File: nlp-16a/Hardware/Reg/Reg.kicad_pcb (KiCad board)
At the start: 2 copper layers, 209.6 x 154.9 mm, 136 parts, among them J1 Conn_02x20_Odd_Even, J2 Conn_02x20_Odd_Even, J3 Conn_02x20_Odd_Even, J4 Conn_02x20_Odd_Even, J5 Conn_02x16_Odd_Even, J6 Conn_02x16_Odd_Even, J7 Screw_Terminal_01x02, J8 Conn_02x10_Odd_Even, U1 CD74HC00, U10 CD74HC00, U11 CD74HC00, U12 CD74HC00, U13 CD74HC00, U14 CD74HC00, U15 CD74HC00, U16 CD74HC00, U17 CD74HC00, U18 CD74HC00, U19 CD74HC00, U2 CD74HC00, U20 CD74HC00, U21 CD74HC00, U22 CD74HC00, U23 CD74HC00, U24 CD74HC00, U25 CD74HC00, U26 CD74HC00, U27 CD74HC00, U28 CD74HC00, U29 CD74HC00, U3 CD74HC00, U30 CD74HC00, U31 CD74HC00, U32 CD74HC00, U33 CD74HC00, U34 CD74HC00, U35 CD74HC00, U4 CD74HC00, U5 CD74HC00, U6 CD74HC00, U7 CD74HC00, U8 CD74HC00, U9 CD74HC00

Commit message: レジスタ基板だいたい完成
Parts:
- added C18: C, Capacitor_THT:C_Disc_D7.5mm_W2.5mm_P5.00mm, F.Cu at (225.4, 53.4)
- added C19: C, Capacitor_THT:C_Disc_D7.5mm_W2.5mm_P5.00mm, F.Cu at (225.4, 66.1)
- added G***: LOGO, LOGO, F.Cu at (190.5, 45.1)
- added JP17: Jumper_3_Bridged12, Jumper:SolderJumper-3_P1.3mm_Bridged12_RoundedPad1.0x1.5mm_NumberLabels, F.Cu at (238.8, 82.5)
- added R36: R, Resistor_SMD:R_0603_1608Metric_Pad0.98x0.95mm_HandSolder, F.Cu at (206.4, 49.5)
- added R37: R, Resistor_SMD:R_0603_1608Metric_Pad0.98x0.95mm_HandSolder, F.Cu at (202.6, 49.5)
- added U36: CD74HC00, Package_DIP:DIP-14_W7.62mm, F.Cu at (228.6, 73.7)
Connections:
- net ALL_SEL_in renamed CLR_in
- D1 pad 2: /Register/Reg0/Q -> Reg_out0
- D10 pad 2: /Register/Reg9/Q -> Reg_out9
- D11 pad 2: /Register/Reg10/Q -> Reg_out10
- D12 pad 2: /Register/Reg11/Q -> Reg_out11
- D13 pad 2: /Register/Reg12/Q -> Reg_out12
- D14 pad 2: /Register/Reg13/Q -> Reg_out13
- D15 pad 2: /Register/Reg14/Q -> Reg_out14
- D16 pad 2: /Register/Reg15/Q -> Reg_out15
- D19 pad 2: Net-(U10-Pad2) -> Net-(U34-Pad11)
- D2 pad 2: /Register/Reg1/Q -> Reg_out1
- D3 pad 2: /Register/Reg2/Q -> Reg_out2
- D4 pad 2: /Register/Reg3/Q -> Reg_out3
- D5 pad 2: /Register/Reg4/Q -> Reg_out4
- D6 pad 2: /Register/Reg5/Q -> Reg_out5
- D7 pad 2: /Register/Reg6/Q -> Reg_out6
- D8 pad 2: /Register/Reg7/Q -> Reg_out7
- D9 pad 2: /Register/Reg8/Q -> Reg_out8
- J1 pad 36: phi1 -> phi1_in
- J3 pad 33: ALL_SEL_out -> CLR_out
- J3 pad 36: phi1 -> phi1_out
- J8 pad 10: Address2 -> Reg_out2
- J8 pad 11: Address11 -> Reg_out11
- J8 pad 12: Address3 -> Reg_out3
- J8 pad 13: Address12 -> Reg_out12
- J8 pad 14: Address4 -> Reg_out4
- J8 pad 15: Address13 -> Reg_out13
- J8 pad 16: Address5 -> Reg_out5
- J8 pad 17: Address14 -> Reg_out14
- J8 pad 18: Address6 -> Reg_out6
- J8 pad 19: Address15 -> Reg_out15
- J8 pad 20: Address7 -> Reg_out7
- J8 pad 5: Address8 -> Reg_out8
- J8 pad 6: Address0 -> Reg_out0
- J8 pad 7: Address9 -> Reg_out9
- J8 pad 8: Address1 -> Reg_out1
- J8 pad 9: Address10 -> Reg_out10
- U1 pad 2: VCC -> Net-(U8-Pad5)
- U1 pad 5: VCC -> Net-(U8-Pad5)
- U10 pad 10: /Register/Reg12/Q -> Reg_out12
- U10 pad 13: /Register/Reg13/Q -> Reg_out13
- U11 pad 10: /Register/Reg10/Q -> Reg_out10
- U11 pad 13: /Register/Reg11/Q -> Reg_out11
- U12 pad 10: /Register/Reg8/Q -> Reg_out8
- U12 pad 13: /Register/Reg9/Q -> Reg_out9
- U13 pad 10: /Register/Reg6/Q -> Reg_out6
- U13 pad 13: /Register/Reg7/Q -> Reg_out7
- U14 pad 10: /Register/Reg4/Q -> Reg_out4
- U14 pad 13: /Register/Reg5/Q -> Reg_out5
- U15 pad 10: /Register/Reg2/Q -> Reg_out2
- U15 pad 13: /Register/Reg3/Q -> Reg_out3
- U16 pad 10: /Register/Reg0/Q -> Reg_out0
- U16 pad 13: /Register/Reg1/Q -> Reg_out1
- U17 pad 10: /Register/Reg15/Q -> Reg_out15
- U17 pad 11: /Register/Reg15/Q -> Reg_out15
- U18 pad 10: /Register/Reg13/Q -> Reg_out13
- U18 pad 11: /Register/Reg13/Q -> Reg_out13
- U19 pad 10: /Register/Reg11/Q -> Reg_out11
- U19 pad 11: /Register/Reg11/Q -> Reg_out11
- U2 pad 2: VCC -> Net-(U8-Pad5)
- U2 pad 5: VCC -> Net-(U8-Pad5)
- U20 pad 10: /Register/Reg9/Q -> Reg_out9
- U20 pad 11: /Register/Reg9/Q -> Reg_out9
- U21 pad 10: /Register/Reg7/Q -> Reg_out7
- U21 pad 11: /Register/Reg7/Q -> Reg_out7
- U22 pad 10: /Register/Reg5/Q -> Reg_out5
- U22 pad 11: /Register/Reg5/Q -> Reg_out5
- U23 pad 10: /Register/Reg3/Q -> Reg_out3
- U23 pad 11: /Register/Reg3/Q -> Reg_out3
- U24 pad 10: /Register/Reg1/Q -> Reg_out1
- U24 pad 11: /Register/Reg1/Q -> Reg_out1
- U25 pad 10: /Register/Reg14/Q -> Reg_out14
- U25 pad 11: /Register/Reg14/Q -> Reg_out14
- U26 pad 10: /Register/Reg12/Q -> Reg_out12
- U26 pad 11: /Register/Reg12/Q -> Reg_out12
- U27 pad 10: /Register/Reg10/Q -> Reg_out10
- U27 pad 11: /Register/Reg10/Q -> Reg_out10
- U28 pad 10: /Register/Reg8/Q -> Reg_out8
- U28 pad 11: /Register/Reg8/Q -> Reg_out8
- U29 pad 10: /Register/Reg6/Q -> Reg_out6
- U29 pad 11: /Register/Reg6/Q -> Reg_out6
- U3 pad 2: VCC -> Net-(U8-Pad5)
- U3 pad 5: VCC -> Net-(U8-Pad5)
- U30 pad 10: /Register/Reg4/Q -> Reg_out4
- U30 pad 11: /Register/Reg4/Q -> Reg_out4
- U31 pad 10: /Register/Reg2/Q -> Reg_out2
- U31 pad 11: /Register/Reg2/Q -> Reg_out2
- U32 pad 10: /Register/Reg0/Q -> Reg_out0
- U32 pad 11: /Register/Reg0/Q -> Reg_out0
- U33 pad 10: ALL_SEL_out -> Net-(U33-Pad5)
- U33 pad 5: ALL_SEL_out -> Net-(U33-Pad5)
- U34 pad 11: Net-(U10-Pad2) -> Net-(U34-Pad11)
- U35 pad 8: ALL_SEL_out -> CLR_out
- U4 pad 2: VCC -> Net-(U8-Pad5)
- U4 pad 5: VCC -> Net-(U8-Pad5)
- U5 pad 2: VCC -> Net-(U8-Pad5)
- U5 pad 5: VCC -> Net-(U8-Pad5)
- U6 pad 2: VCC -> Net-(U8-Pad5)
- U6 pad 5: VCC -> Net-(U8-Pad5)
- U7 pad 2: VCC -> Net-(U8-Pad5)
- U7 pad 5: VCC -> Net-(U8-Pad5)
- U8 pad 2: VCC -> Net-(U8-Pad5)
- U8 pad 5: VCC -> Net-(U8-Pad5)
- U9 pad 10: /Register/Reg14/Q -> Reg_out14
- U9 pad 13: /Register/Reg15/Q -> Reg_out15
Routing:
- net Net-(U34-Pad11): track 0.00 -> 328.5 mm, vias 0 -> 2
- net Net-(U8-Pad5): track 0.00 -> 266.3 mm
- net Reg_out1: track 0.00 -> 179.0 mm, vias 0 -> 2
- net Reg_out0: track 0.00 -> 177.6 mm, vias 0 -> 2
- net Reg_out3: track 0.00 -> 174.7 mm, vias 0 -> 2
- net Reg_out2: track 0.00 -> 173.8 mm, vias 0 -> 2
- net Reg_out5: track 0.00 -> 167.9 mm, vias 0 -> 2
- net Reg_out4: track 0.00 -> 167.3 mm, vias 0 -> 2
- net Reg_out14: track 0.00 -> 165.8 mm, vias 0 -> 3
- net Reg_out7: track 0.00 -> 165.6 mm, vias 0 -> 2
- net Reg_out6: track 0.00 -> 165.6 mm, vias 0 -> 2
- net Reg_out15: track 0.00 -> 165.2 mm, vias 0 -> 3
- net CLR_out: track 0.00 -> 162.4 mm, vias 0 -> 1
- net ALL_SEL_out: track 158.3 -> 0.00 mm, vias 1 -> 0
- net /Register/Reg14/Q: track 157.0 -> 0.00 mm
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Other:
- board text added: "+ -"
- board text added: "0 --------------ID-------------- F"
- board text added: "0 -------------ID--------------- F"
- board text added: "0 ------------Data------------- F 0 -----------Address------------ F"
- board text added: "16bit Reg"
- board text added: "3 2 1 0"
- board text added: "7 6 5 4"
- board text added: "A BUS"
- board text added: "ALL φ1 φ2"
- board text added: "B A 9 8"
- board text added: "B D x x"
- board text added: "Buf, Data CLR"
- board text added: "Ctrl"
- board text added: "Data"
- board text added: "F ------------- 8 7 ------------- 0"
- board text added: "F E D C"
- board text added: "MUX"
- board text added: "NLP-16A 16bit Register v1.0 S/N:007-0001"
- board text added: "PWR"
- board text added: "RD"
- board text added: "Reg OUTPUT PORT"
- board text added: "Vcc GND"
- board text added: "WR"
- board text added: "Y BUS"
- board text added: "unbuf : short"
- board text added: "↑IR2 short 2-3 cut 1-2"

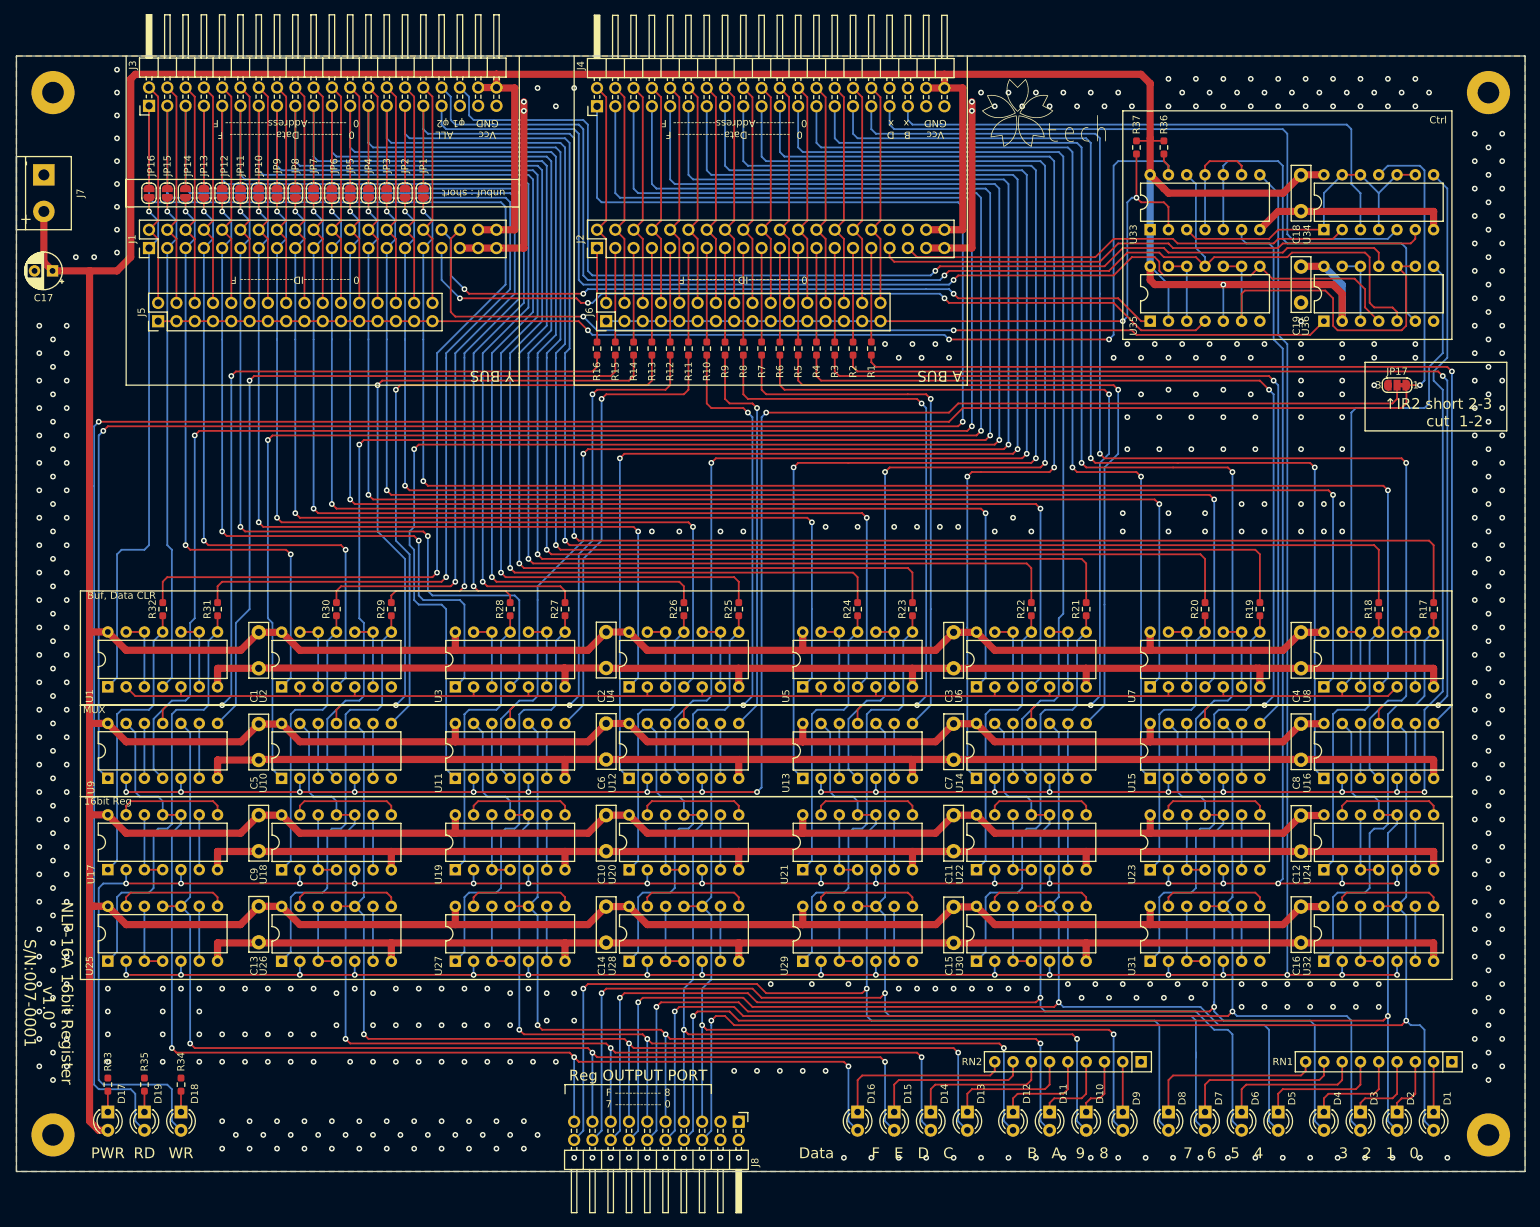
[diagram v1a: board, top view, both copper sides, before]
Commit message: テストを受けてレジスタの設計を更新
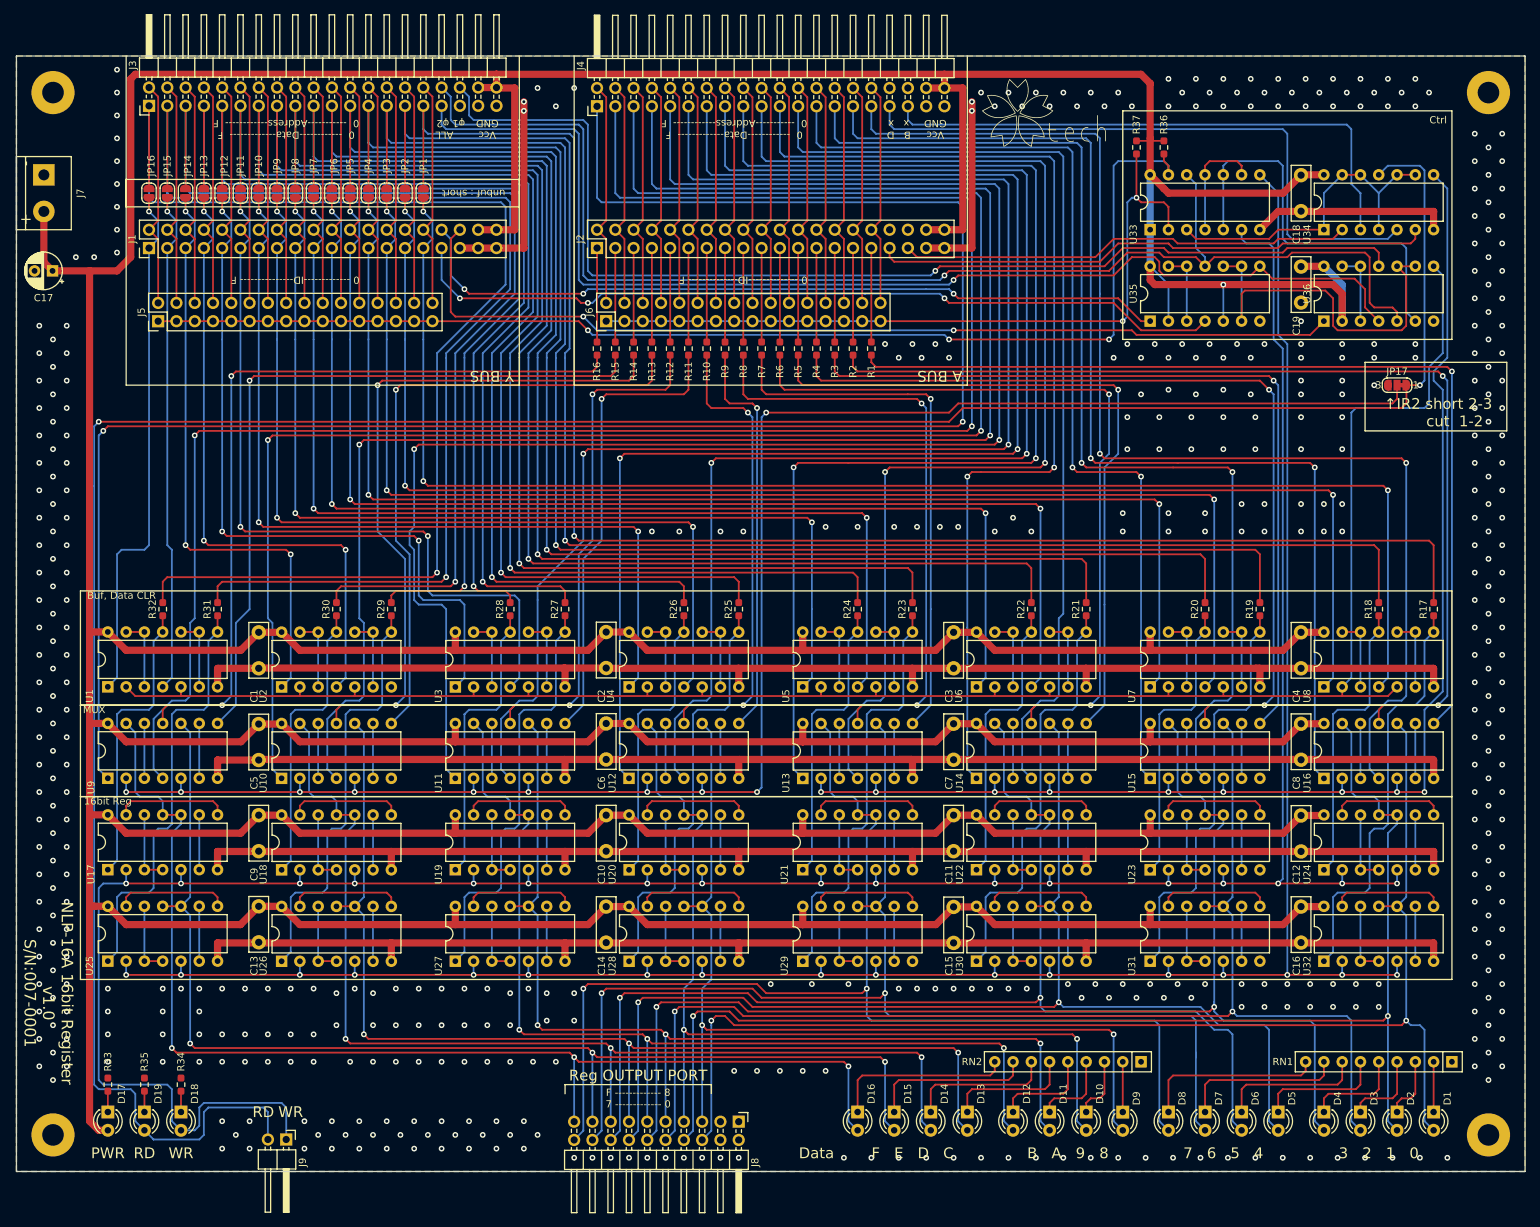
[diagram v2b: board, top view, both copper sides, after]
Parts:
- added J9: Conn_01x02_Male, Connector_PinHeader_2.54mm:PinHeader_1x02_P2.54mm_Horizontal, F.Cu at (84.5, 187.3)
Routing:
- net Net-(D19-Pad2): track 328.5 -> 354.0 mm
- net /Register/Reg1/Gate: track 350.0 -> 372.4 mm
- net GND: vias 499 -> 495

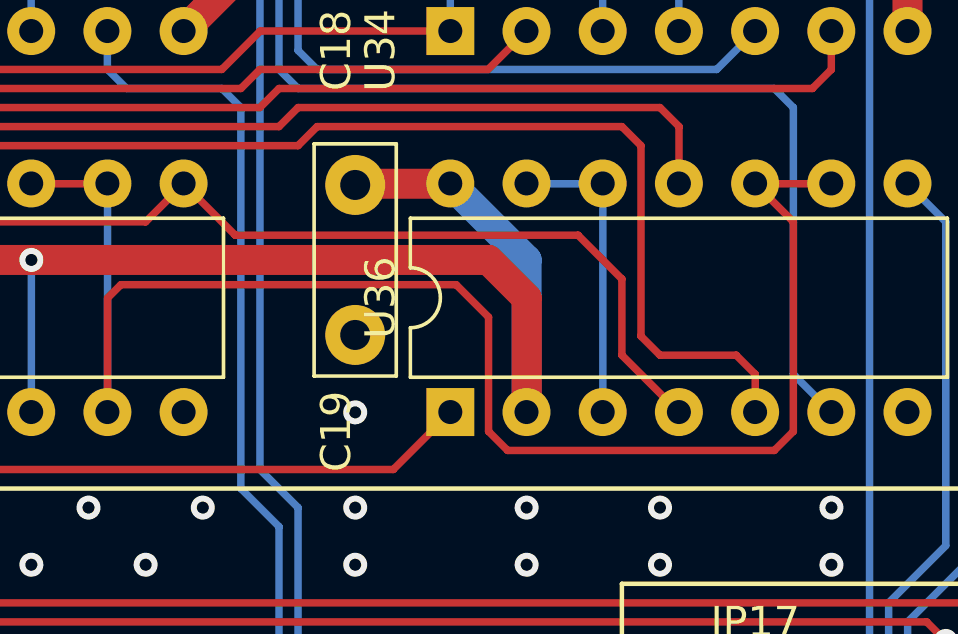
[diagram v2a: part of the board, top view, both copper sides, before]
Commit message: レジスタクリア時の動作を修正
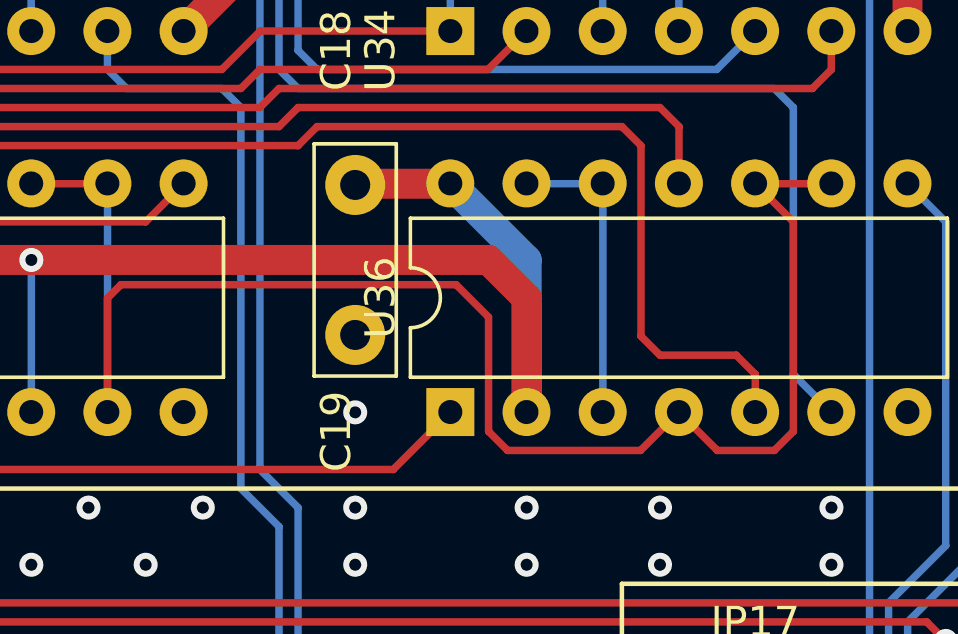
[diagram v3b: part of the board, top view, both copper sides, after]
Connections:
- net CLR_in renamed ~CLR_in
- J3 pad 33: CLR_out -> ~CLR_out
- U35 pad 10: Net-(U35-Pad10) -> CLR
- U35 pad 6: Net-(U35-Pad10) -> CLR
- U35 pad 8: CLR_out -> ~CLR_out
- U35 pad 9: Net-(U35-Pad10) -> CLR
- U36 pad 10: Net-(U35-Pad10) -> CLR
- U36 pad 4: CLR_out -> CLR
- U36 pad 9: Net-(U35-Pad10) -> CLR
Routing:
- net CLR_out: track 162.4 -> 0.00 mm, vias 1 -> 0
- net ~CLR_out: track 0.00 -> 141.3 mm, vias 0 -> 1
- net CLR: track 0.00 -> 54.2 mm
- net Net-(U35-Pad10): track 53.1 -> 0.00 mm
